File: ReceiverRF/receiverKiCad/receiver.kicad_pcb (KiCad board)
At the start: 2 copper layers, 100 x 116.7 mm, 87 parts, among them J1 RF2-03E-T-00-50-G, J2 Conn_01x05_Socket, J3 Conn_01x02_Socket, J4 Conn_01x04, Q1 MMBT3904, Q2 NTR4101PT1G, SW1 SW_Push, SW2 SW_Push, SW3 SW_Push, SW4 SW_Push, SW5 SW_SPDT, U1 STM32F103RET6, U2 NCV5501DT33RKG, U3 NJM2882F05-TE1, U4 MLX90393SLW-ABA-011-RE, U5 TXS0102DCUR, Y1 406C35D08M00000

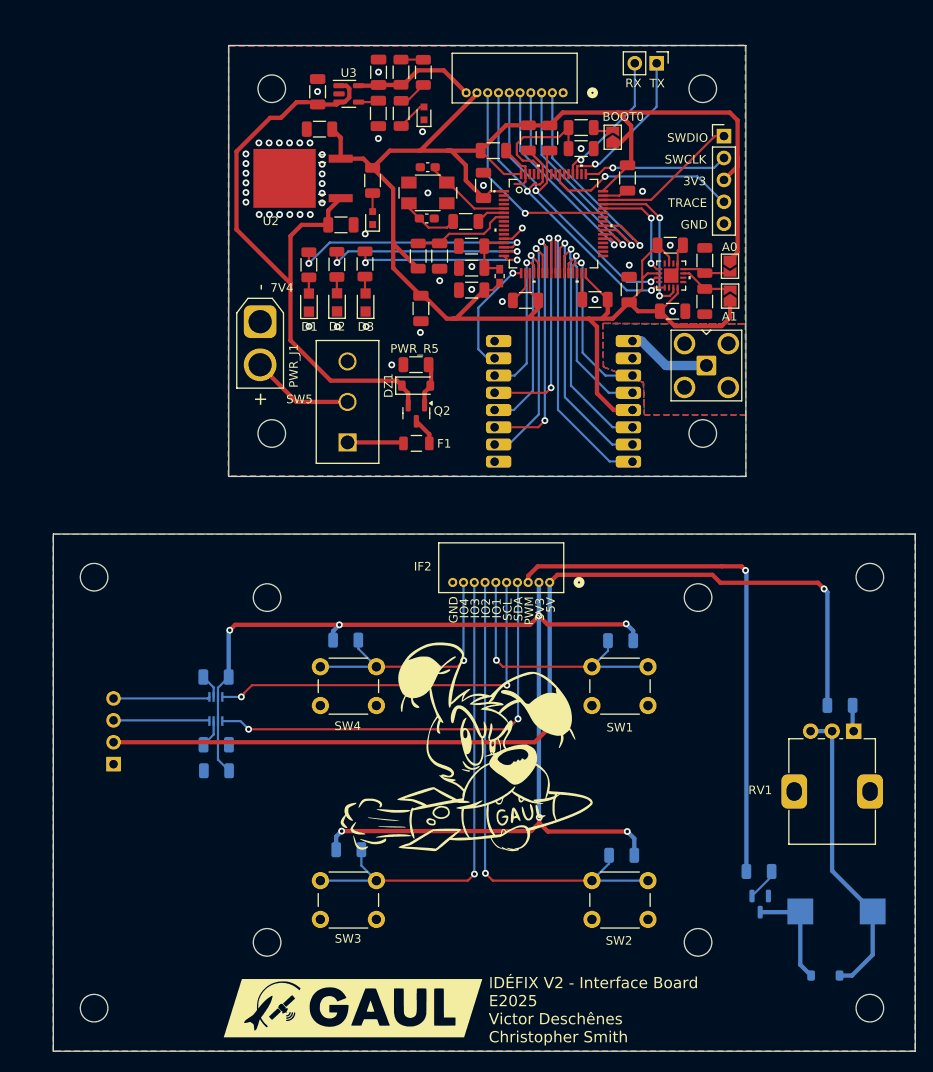
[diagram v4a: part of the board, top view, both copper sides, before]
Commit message: Refactor timer handling and add TRANSMIT/RECEIVE definition macros
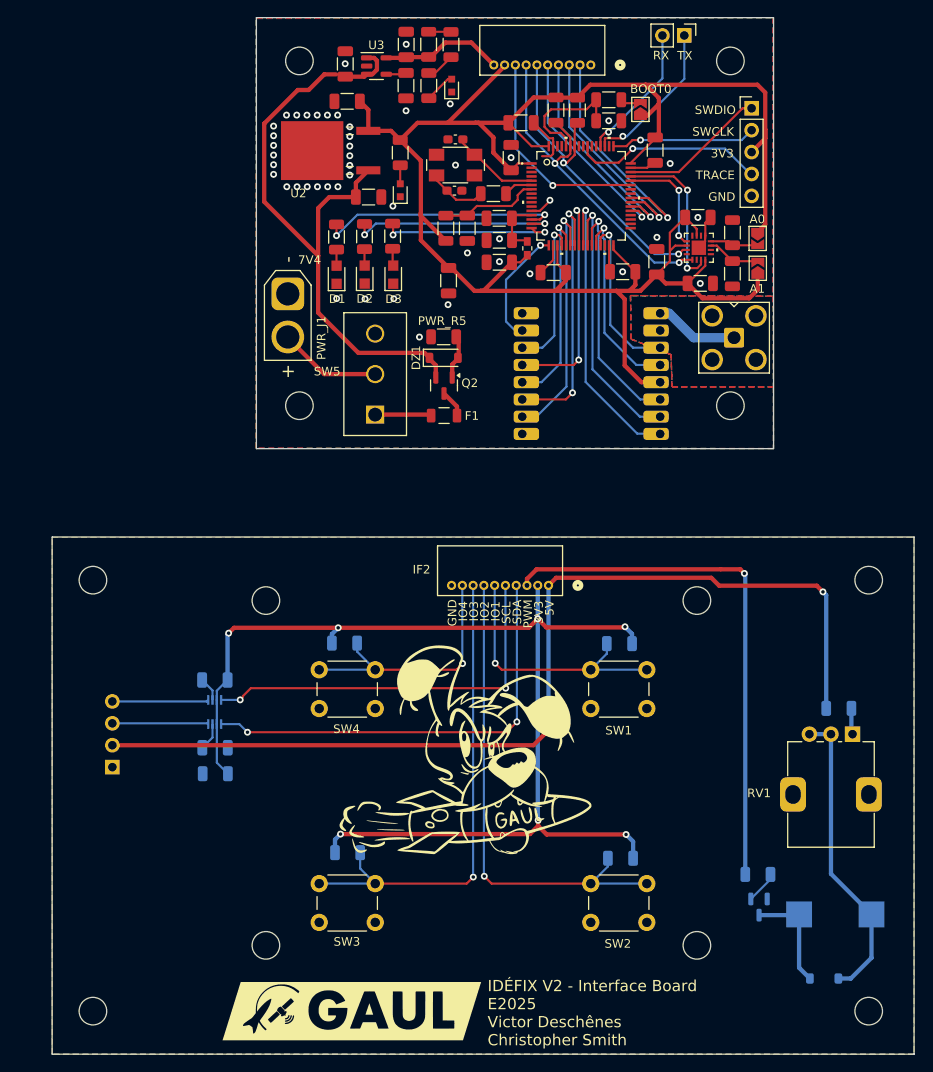
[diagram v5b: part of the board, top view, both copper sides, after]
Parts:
- removed the G*** at (153.6, 119.8)
- removed the G*** at (140.2, 150.5)
- removed the G*** at (165.8, 53.9)
- removed the G*** at (141.0, 56.5)
- added G***: LOGO, Footprints:logo, F.Cu at (140.1, 150.9)
- added G***: LOGO, LOGO, F.Cu at (153.4, 120.1)
- added G***: LOGO, Footprints:logo, B.Cu at (169.0, 50.7)
- added G***: LOGO, LOGO, B.Cu at (144.2, 53.3)
- moved I2C_R2 4.55 mm to (166.2, 46.4)
- moved PWR_R3 4.55 mm to (151.6, 38.8)
- moved STM_C8 4.55 mm to (157.2, 61.5)
- moved U2 4.55 mm to (135.5, 51.1)
- moved D1 4.55 mm to (138.3, 65.5)
- moved F1 4.55 mm to (150.8, 81.8)
- moved HOLES1 4.55 mm to (159.0, 60.7)
- moved I2C_R1 4.55 mm to (163.7, 46.4)
- moved J1 4.55 mm to (184.4, 72.8)
- moved JP1 4.55 mm to (173.5, 46.3)
- moved MLX_A0 4.55 mm to (187.1, 61.2)
- moved MLX_C2 4.55 mm to (180.2, 58.8)
- moved MLX_C3 4.55 mm to (151.3, 66.1)
- moved PWR_C1 4.55 mm to (142.0, 56.4)
- moved PWR_C2 4.55 mm to (139.5, 45.3)
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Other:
- board size 100 x 116.7 mm -> 100 x 120.3 mm
